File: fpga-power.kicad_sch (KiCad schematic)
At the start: 100 parts, among them U15 XC7K160T-FFG676

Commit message: Update PCB naming
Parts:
- C11, C143, C21, C231, C276, C277, C278, C279, C286, C294, C295, C296, C297, C298, C299, C300, C301, C302, C303, C304, C305, C306, C307, C308, C309, C310, C32, C34, C43, C44, C47, C48, C49, C50, C51, C52, C53, C54, C55, C56, C57, C58, C59, C60, C61, C62, C63, C64, C65, C66, C67, C68, C69, C70, C71, C72, C73, C74, C75, C76, C77, C79, C82, C83, C84, C85, C86, C87, C88, C89, C9, C90, C91, C92, C93, C94, C95: footprint data-center-dram-tester-footprints:0201-res -> data-center-rdimm-ddr4-tester-footprints:0201-res; symbol data-center-dram-tester:C_100n_0201 -> data-center-rdimm-ddr4-tester:C_100n_0201
- C114, C15, C22, C23, C24, C25, C3, C6, C78, C80, C81: footprint data-center-dram-tester-footprints:0603-cap -> data-center-rdimm-ddr4-tester-footprints:0603-cap; symbol data-center-dram-tester:C_47u_0603 -> data-center-rdimm-ddr4-tester:C_47u_0603
- C115, C14, C144, C16, C17, C19, C7: footprint data-center-dram-tester-footprints:0402-cap -> data-center-rdimm-ddr4-tester-footprints:0402-cap; symbol data-center-dram-tester:C_4u7_0402 -> data-center-rdimm-ddr4-tester:C_4u7_0402
- C20: footprint data-center-dram-tester-footprints:KEMET_A -> data-center-rdimm-ddr4-tester-footprints:KEMET_A; symbol data-center-dram-tester:C_100u_KEMET_A -> data-center-rdimm-ddr4-tester:C_100u_KEMET_A
- C26, C8: footprint data-center-dram-tester-footprints:KEMET_D -> data-center-rdimm-ddr4-tester-footprints:KEMET_D; symbol data-center-dram-tester:C_330u_KEMET_D -> data-center-rdimm-ddr4-tester:C_330u_KEMET_D
- C313: footprint data-center-dram-tester-footprints:0402-cap -> data-center-rdimm-ddr4-tester-footprints:0402-cap; symbol data-center-dram-tester:C_100n_0402 -> data-center-rdimm-ddr4-tester:C_100n_0402
- U15: footprint data-center-dram-tester-footprints:xc7k160tfbg676 -> data-center-rdimm-ddr4-tester-footprints:xc7k160tfbg676; symbol data-center-dram-tester:XC7K160T-FFG676 -> data-center-rdimm-ddr4-tester:XC7K160T-FFG676
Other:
- title: Data Center DRAM Tester -> Data Center RDIMM DDR4 Tester

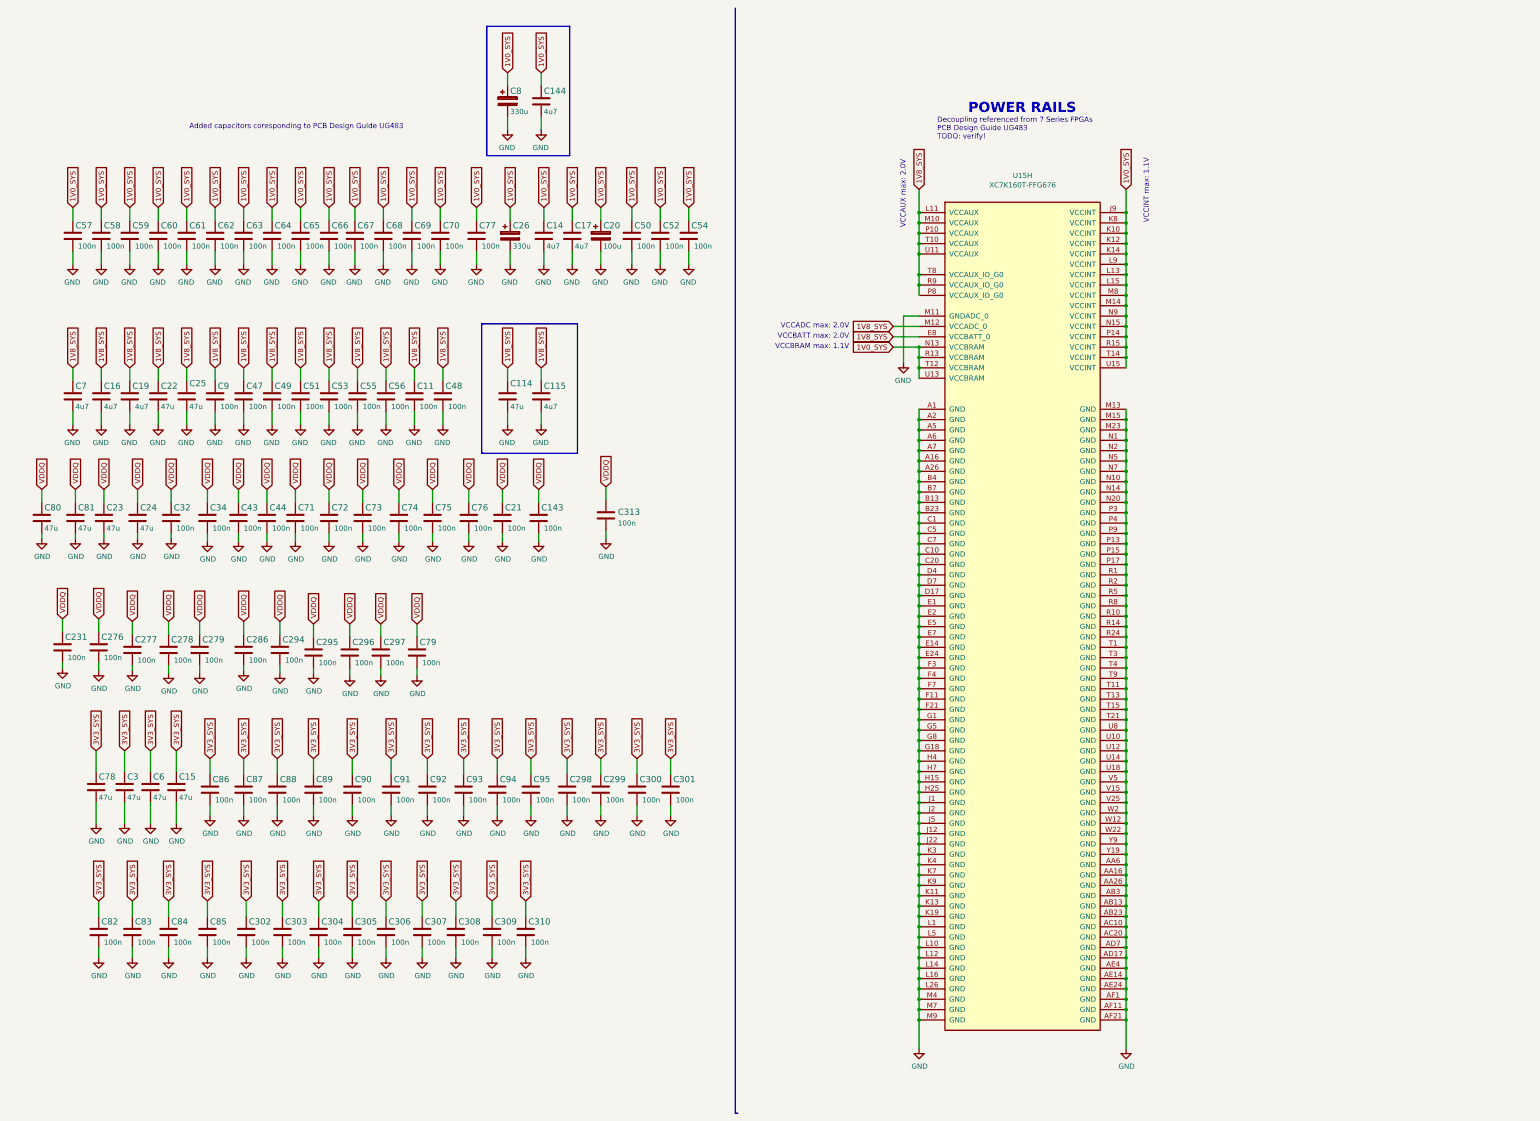
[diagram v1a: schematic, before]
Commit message: Introduce component standardization
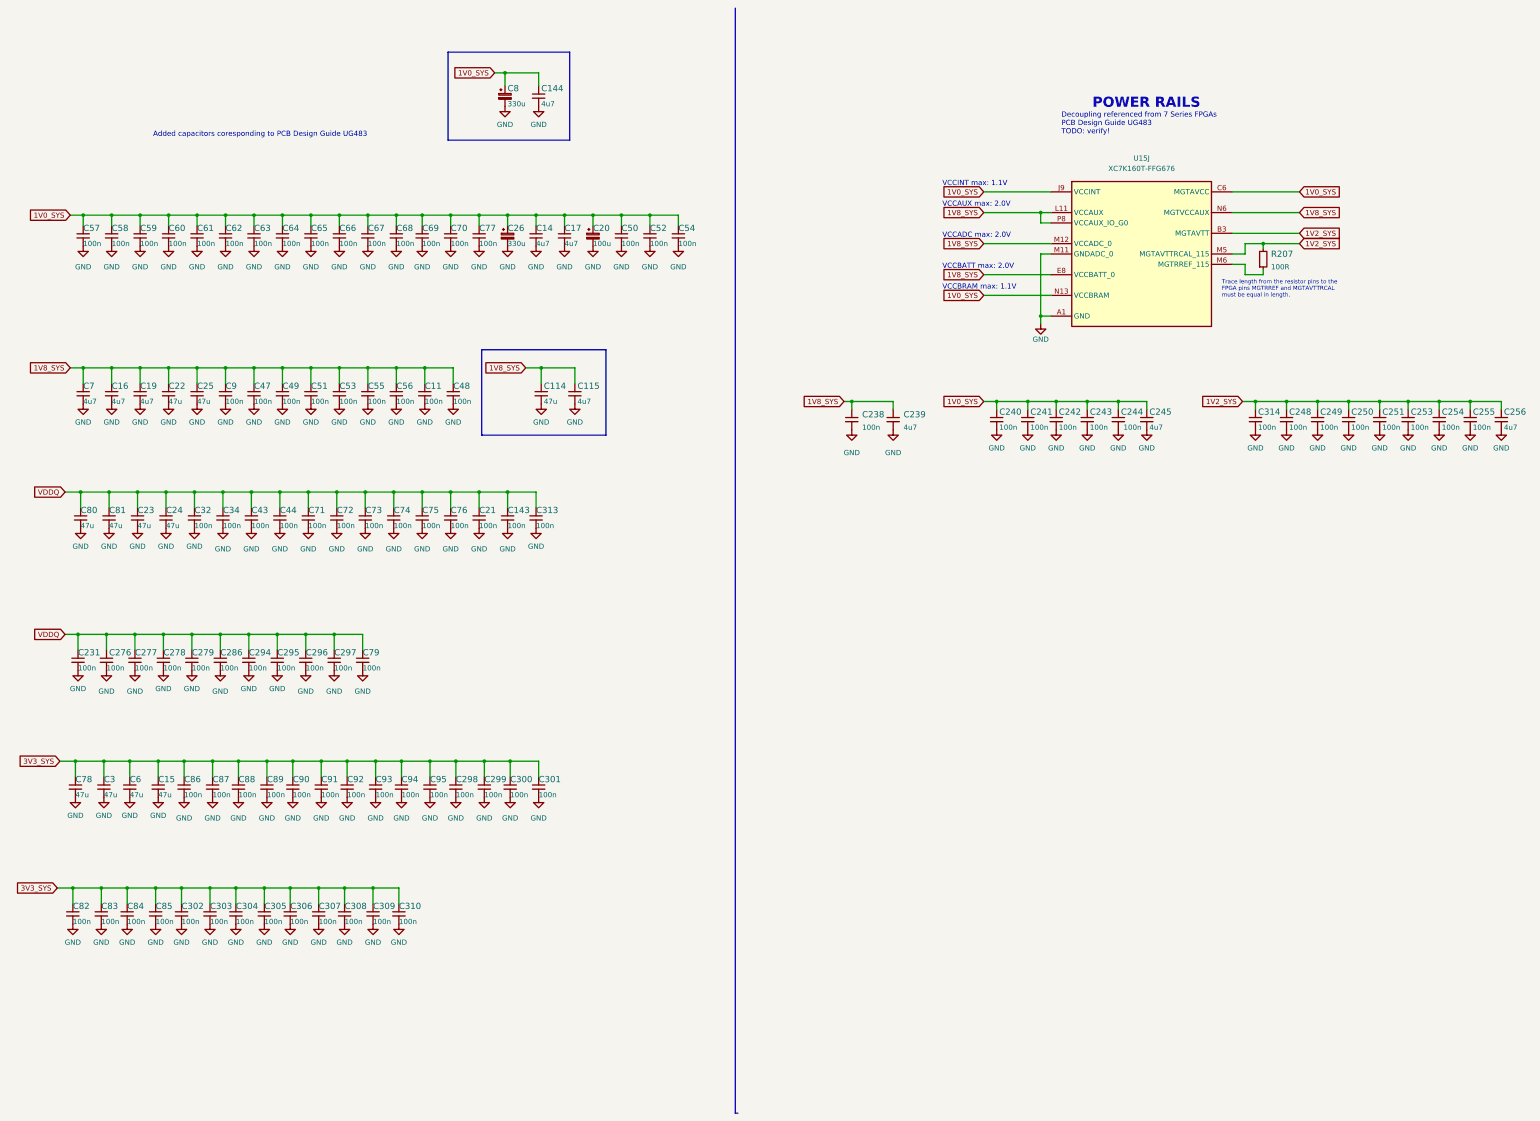
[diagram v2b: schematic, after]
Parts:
- added C238, C240, C241, C242, C243, C244, C248, C249, C250, C251, C253, C254, C255: C_100n_0201, data-center-rdimm-ddr4-tester-footprints:C_0201, symbol data-center-rdimm-ddr4-tester:C_100n_0201
- added C239, C245, C256: C_4u7_0402, data-center-rdimm-ddr4-tester-footprints:C_0402_1005Metric, symbol data-center-rdimm-ddr4-tester:C_4u7_0402
- added C314: C_100n_0402, data-center-rdimm-ddr4-tester-footprints:C_0402_1005Metric, symbol data-center-rdimm-ddr4-tester:C_100n_0402
- added R207: R_100R_0402, data-center-rdimm-ddr4-tester-footprints:R_0402_1005Metric, symbol data-center-rdimm-ddr4-tester:R_100R_0402
- C11, C143, C21, C231, C276, C277, C278, C279, C286, C294, C295, C296, C297, C298, C299, C300, C301, C302, C303, C304, C305, C306, C307, C308, C309, C310, C32, C34, C43, C44, C47, C48, C49, C50, C51, C52, C53, C54, C55, C56, C57, C58, C59, C60, C61, C62, C63, C64, C65, C66, C67, C68, C69, C70, C71, C72, C73, C74, C75, C76, C77, C79, C82, C83, C84, C85, C86, C87, C88, C89, C9, C90, C91, C92, C93, C94, C95: footprint data-center-rdimm-ddr4-tester-footprints:0201-res -> data-center-rdimm-ddr4-tester-footprints:C_0201; Author (none) -> Antmicro; License (none) -> Apache-2.0; Manufacturer YAGEO -> Yaego
- C114, C15, C22, C23, C24, C25, C3, C6, C78, C80, C81: footprint data-center-rdimm-ddr4-tester-footprints:0603-cap -> data-center-rdimm-ddr4-tester-footprints:C_0603_1608Metric; Author (none) -> Antmicro; License (none) -> Apache-2.0; Manufacturer MURATA -> Murata
- C115, C14, C144, C16, C17, C19, C7: footprint data-center-rdimm-ddr4-tester-footprints:0402-cap -> data-center-rdimm-ddr4-tester-footprints:C_0402_1005Metric; Author (none) -> Antmicro; License (none) -> Apache-2.0; Manufacturer MURATA -> Murata
- C20: Author (none) -> Antmicro; License (none) -> Apache-2.0; Manufacturer VISHAY -> Vishay
- C26, C8: Author (none) -> Antmicro; License (none) -> Apache-2.0
- C313: footprint data-center-rdimm-ddr4-tester-footprints:0402-cap -> data-center-rdimm-ddr4-tester-footprints:C_0402_1005Metric; Author (none) -> Antmicro; Dielectric (none) -> X5R; License (none) -> Apache-2.0; Voltage (none) -> 50V
- U15: footprint data-center-rdimm-ddr4-tester-footprints:xc7k160tfbg676 -> data-center-rdimm-ddr4-tester-footprints:BGA-676_27x27mm_Layout26x26_P1X1mm; Author (none) -> Antmicro; License (none) -> Apache-2.0; MPN (none) -> XC7K160T-FFG676; Manufacturer (none) -> Xilinx
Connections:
- net 1V0_SYS: now also U15.C6 (MGTAVCC), U15.E6 (MGTAVCC), U15.G6 (MGTAVCC), U15.J6 (MGTAVCC), U15.L6 (MGTAVCC), C240.1, C241.1, C242.1, C243.1, C244.1, C245.1
- net 1V8_SYS: now also U15.N6 (MGTVCCAUX), C238.1, C239.1
- net GND: now also C238.2, C239.2, C240.2, C241.2, C242.2, C243.2, C244.2, C245.2, C248.2, C249.2, C250.2, C251.2, C253.2, C254.2, C255.2, C256.2, C314.2
- new net: R207.1, U15.M6 (MGTRREF_115)
- new net 1V2_SYS: C248.1, C249.1, C250.1, C251.1, C253.1, C254.1, C255.1, C256.1, C314.1, R207.2, U15.B3 (MGTAVTT), U15.C2 (MGTAVTT), U15.D3 (MGTAVTT), U15.G2 (MGTAVTT), U15.H3 (MGTAVTT), U15.L2 (MGTAVTT), U15.M3 (MGTAVTT), U15.M5 (MGTAVTTRCAL_115)
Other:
- note added: "Trace length from the resistor pins to the FPGA pins MGTRREF and MGTAVTTRCAL must be equal in length."
- moved on the sheet: C11, C114, C115, C14, C143, C144, C15, C16, C17, C19, C21, C22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

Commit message: [#55119] component update
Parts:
- C11, C143, C21, C231, C238, C240, C241, C242, C243, C244, C248, C249, C250, C251, C253, C254, C255, C276, C277, C278, C279, C286, C294, C295, C296, C297, C298, C299, C300, C301, C302, C303, C304, C305, C306, C307, C308, C309, C310, C32, C34, C43, C44, C47, C48, C49, C50, C51, C52, C53, C54, C55, C56, C57, C58, C59, C60, C61, C62, C63, C64, C65, C66, C67, C68, C69, C70, C71, C72, C73, C74, C75, C76, C77, C79, C82, C83, C84, C85, C86, C87, C88, C89, C9, C90, C91, C92, C93, C94, C95: footprint data-center-rdimm-ddr4-tester-footprints:C_0201 -> antmicro-footprints:C_0201; symbol data-center-rdimm-ddr4-tester:C_100n_0201 -> antmicroCapacitorsmisc:C_100n_0201
- C114, C15, C22, C23, C24, C25, C3, C6, C78, C80, C81: footprint data-center-rdimm-ddr4-tester-footprints:C_0603_1608Metric -> antmicro-footprints:C_0603_1608Metric; symbol data-center-rdimm-ddr4-tester:C_47u_0603 -> antmicroCapacitors0603:C_47u_0603
- C115, C14, C144, C16, C17, C19, C239, C245, C256, C7: footprint data-center-rdimm-ddr4-tester-footprints:C_0402_1005Metric -> antmicro-footprints:C_0402_1005Metric; symbol data-center-rdimm-ddr4-tester:C_4u7_0402 -> antmicroCapacitors0402:C_4u7_0402
- C313, C314: footprint data-center-rdimm-ddr4-tester-footprints:C_0402_1005Metric -> antmicro-footprints:C_0402_1005Metric; symbol data-center-rdimm-ddr4-tester:C_100n_0402 -> antmicroCapacitors0402:C_100n_0402
- R207: footprint data-center-rdimm-ddr4-tester-footprints:R_0402_1005Metric -> antmicro-footprints:R_0402_1005Metric; symbol data-center-rdimm-ddr4-tester:R_100R_0402 -> antmicroResistors0402:R_100R_0402
- U15: footprint data-center-rdimm-ddr4-tester-footprints:BGA-676_27x27mm_Layout26x26_P1X1mm -> antmicro-footprints:BGA-676_27x27mm_Layout26x26_P1X1mm; symbol data-center-rdimm-ddr4-tester:XC7K160T-FFG676 -> antmicroMicrocontrollers:XC7K160T-FFG676; Manufacturer Xilinx -> AMD-Xilinx
